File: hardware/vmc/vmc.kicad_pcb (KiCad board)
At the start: 2 copper layers, 63 x 29 mm, 37 parts, among them J1 Conn_01x05_Pin, J2 push button, J3 BUS, M1 F130, Q1 BSS123, U1 SHT31-DIS, U2 PIC18F05Q40, U4 MCP2003B, U5 uA7805, U6 MAX22201

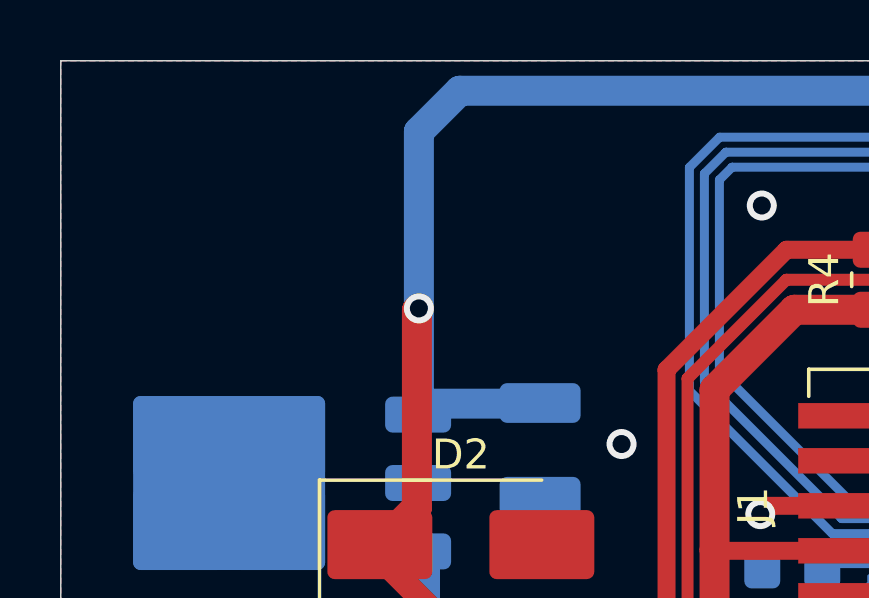
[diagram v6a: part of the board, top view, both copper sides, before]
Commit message: hardware/vmc: convert a via to testpoint, so we can have a true PTH
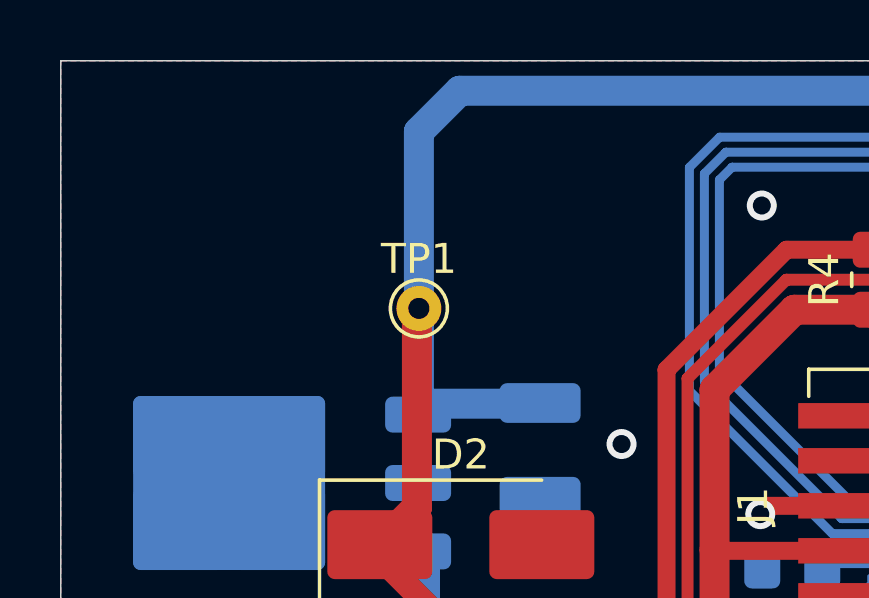
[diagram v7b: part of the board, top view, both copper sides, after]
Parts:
- added TP1: TestPoint, TestPoint:TestPoint_THTPad_D1.5mm_Drill0.7mm, F.Cu at (111.9, 58.3)
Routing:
- net /+12V: vias 2 -> 1
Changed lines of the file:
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@@
 		)
 	)
+	(footprint "TestPoint:TestPoint_THTPad_D1.5mm_Drill0.7mm"
+		(layer "F.Cu")
+		(at 111.938 58.255)
+		(descr "THT pad as test Point, diameter 1.5mm, hole diameter 0.7mm")
+		(tags "test point THT pad")
+		(property "Reference" "TP1"
+			(at 0 -1.648 0)
+			(layer "F.SilkS")
+			(effects
+				(font
+					(size 1 1)
+					(thickness 0.15)
+				)
+			)
+		)
+		(property "Value" "TestPoint"
+			(at 0 1.75 0)
+			(layer "F.Fab")
+			(effects
+				(font
+					(size 1 1)
+					(thickness 0.15)
+				)
+			)
+		)
+		(property "Footprint" "TestPoint:TestPoint_THTPad_D1.5mm_Drill0.7mm"
+			(at 0 0 0)
+			(unlocked yes)
+			(layer "F.Fab")
+			(hide yes)
+			(effects
+				(font
+					(size 1.27 1.27)
+					(thickness 0.15)
+				)
+			)
+		)
+		(property "Datasheet" ""
+			(at 0 0 0)
+			(unlocked yes)
+			(layer "F.Fab")
+			(hide yes)
+			(effects
+				(font
+					(size 1.27 1.27)
+					(thickness 0.15)
+				)
+			)
+		)
+		(property "Description" "test point"
+			(at 0 0 0)
+			(unlocked yes)
+			(layer "F.Fab")
+			(hide yes)
+			(effects
+				(font
+					(size 1.27 1.27)
+					(thickness 0.15)
+				)
+			)
+		)
+		(property ki_fp_filters "Pin* Test*")
+		(sheetname "Root")
+		(sheetfile "vmc.kicad_sch")
+		(attr exclude_from_pos_files)
+		(fp_circle
+			(center 0 0)
+			(end 0 0.95)
+			(stroke
+				(width 0.12)
+				(type solid)
+			)
+			(fill none)
+			(layer "F.SilkS")
+		)
+		(fp_circle
+			(center 0 0)
+			(end 1.25 0)
+			(stroke
+				(width 0.05)
+				(type solid)
+			)
+			(fill none)
+			(layer "F.CrtYd")
+		)
+		(fp_text user "${REFERENCE}"
+			(at 0 -1.65 0)
+			(layer "F.Fab")
+			(effects
+				(font
+					(size 1 1)
+					(thickness 0.15)
+				)
+			)
+		)
+		(pad "1" thru_hole circle
+			(at 0 0)
+			(size 1.5 1.5)
+			(drill 0.7)
+			(layers "*.Cu" "*.Mask")
+			(remove_unused_layers no)
+			(net 4 "/+12V")
+			(pinfunction "1")
+			(pintype "passive")
+		)
+	)
 	(footprint "conn-local:Molex_Pico-SPOX-5-Vertical"
 		(layer "F.Cu")
@@
 		(size 1)
 		(drill 0.6)
-		(layers "F.Cu" "B.Cu")
-		(net 4)
-	)
-	(via
-		(at 111.938 58.255)
-		(size 1)
-		(drill 0.6)
